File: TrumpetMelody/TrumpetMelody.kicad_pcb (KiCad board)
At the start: 2 copper layers, 76.2 x 68.6 mm, 81 parts, among them J1 USB_B_Micro, J2 Conn_01x05, J3 640456-3, J4 640456-3, SW1 SW_Push, U1 STM32F411RETx, U2 TLV62565DBVR, U3 MAX98357AETE_T, U4 MAX7375AXR805

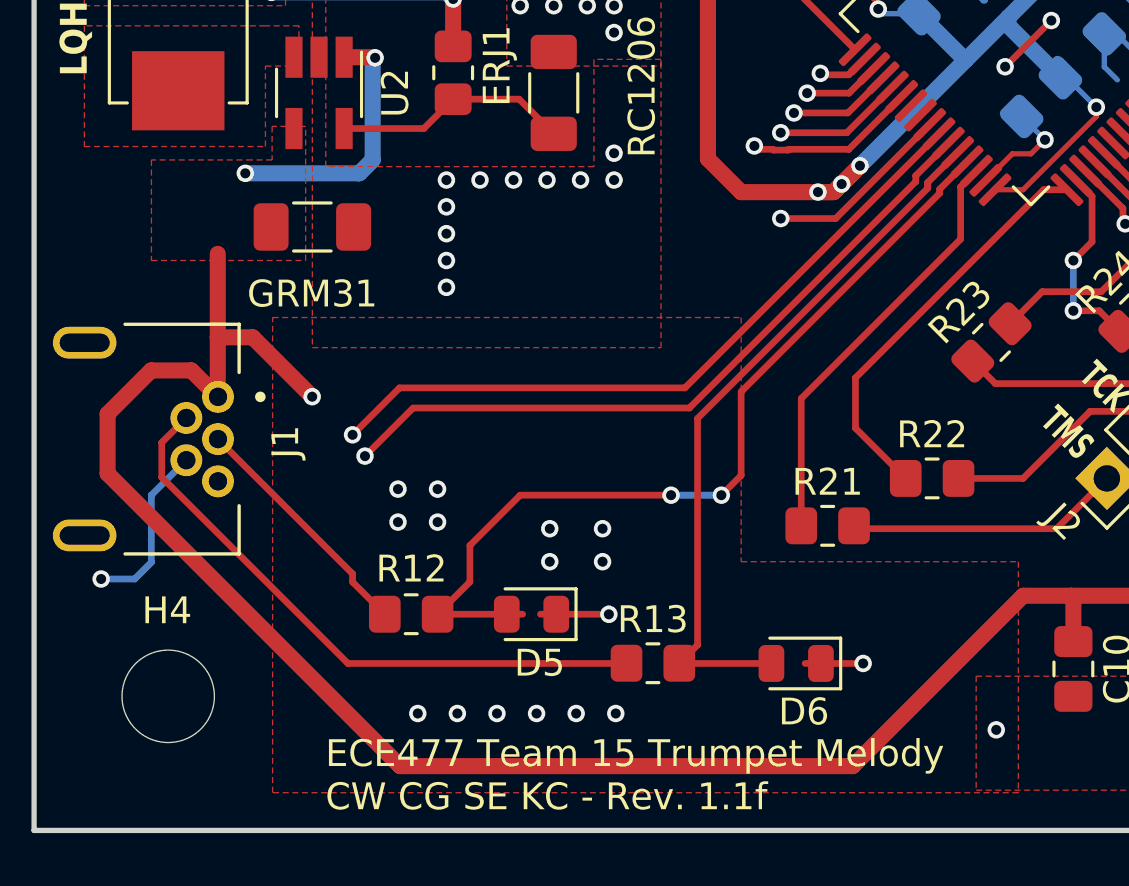
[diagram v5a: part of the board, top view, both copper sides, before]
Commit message: New ESD protection on USB and verified
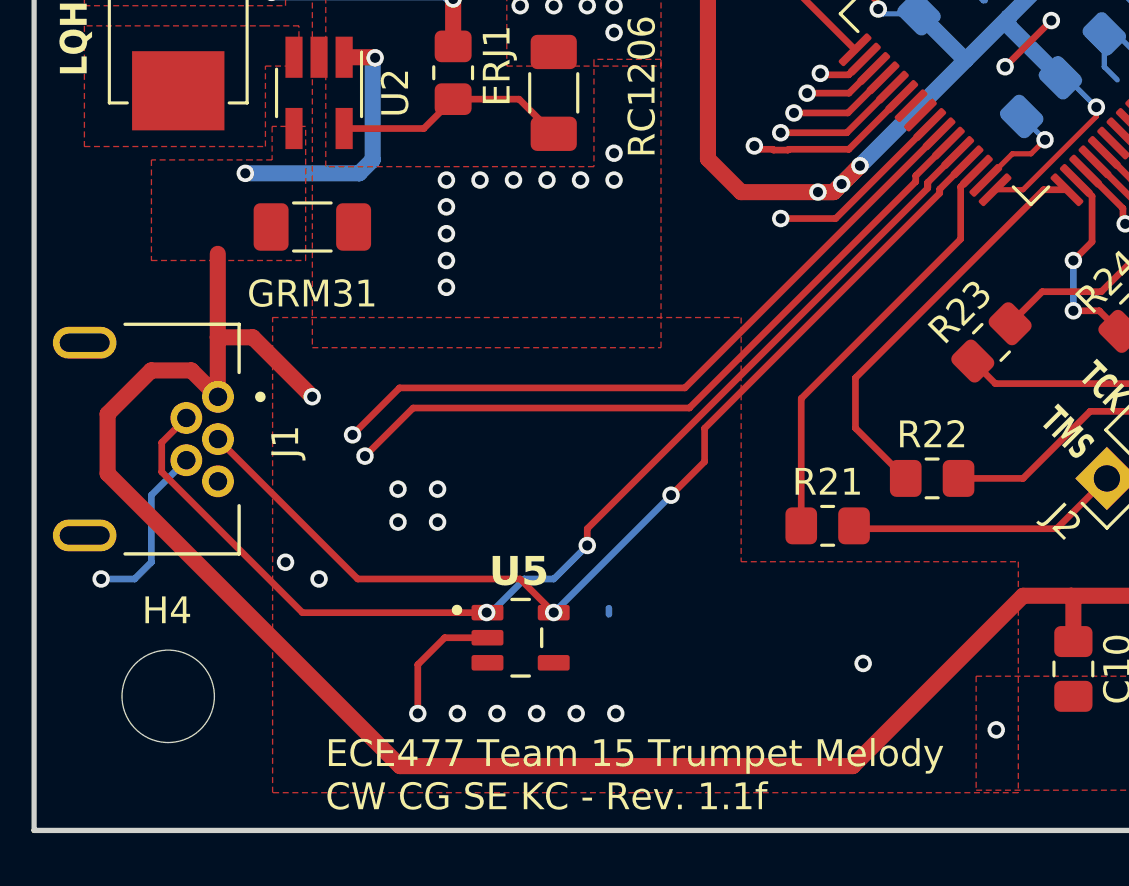
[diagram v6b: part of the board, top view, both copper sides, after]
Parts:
- removed D5, D6: D_TVS, Diode_SMD:D_0805_2012Metric
- removed R12, R13: 220, Resistor_SMD:R_0805_2012Metric_Pad1.20x1.40mm_HandSolder
- added U5: ESDS304DBVR, TrumpetMelodyFootprintLibrary:SOT95P280X145-5N, F.Cu at (165.8, 107.0)
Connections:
- J1 pad 2: Net-(J1-D-) -> USB_DM
- J1 pad 3: Net-(J1-D+) -> USB_DP
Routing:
- net Net-(J1-D-): track 23.6 -> 0.00 mm
- net USB_DM: track 27.4 -> 42.8 mm, vias 0 -> 2
- net Net-(J1-D+): track 9.26 -> 0.00 mm
- net USB_DP: track 33.1 -> 39.0 mm
- net GND: track 54.6 -> 54.7 mm, vias 146 -> 143

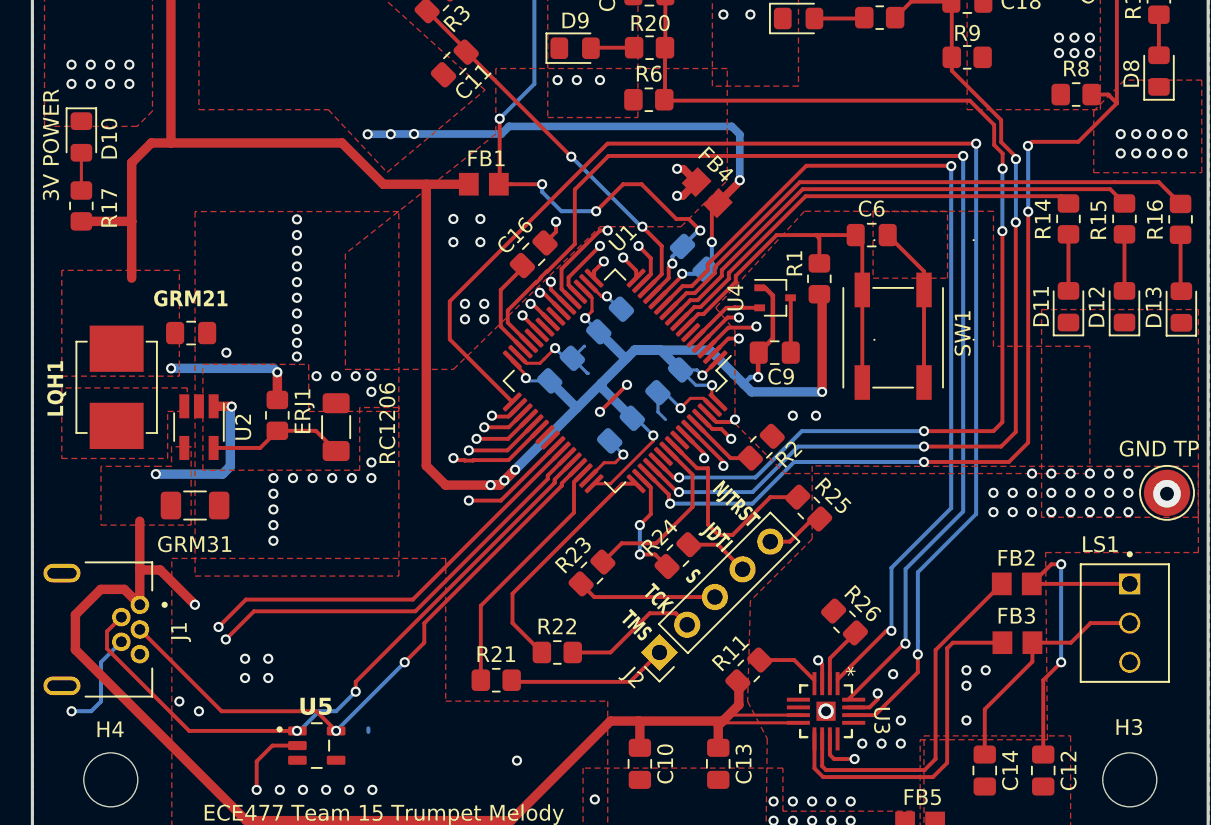
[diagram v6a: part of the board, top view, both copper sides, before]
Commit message: changes to DP/DM signals to reduce via usage/turns, slight change to the button 0 routing bc i saw an acute angle
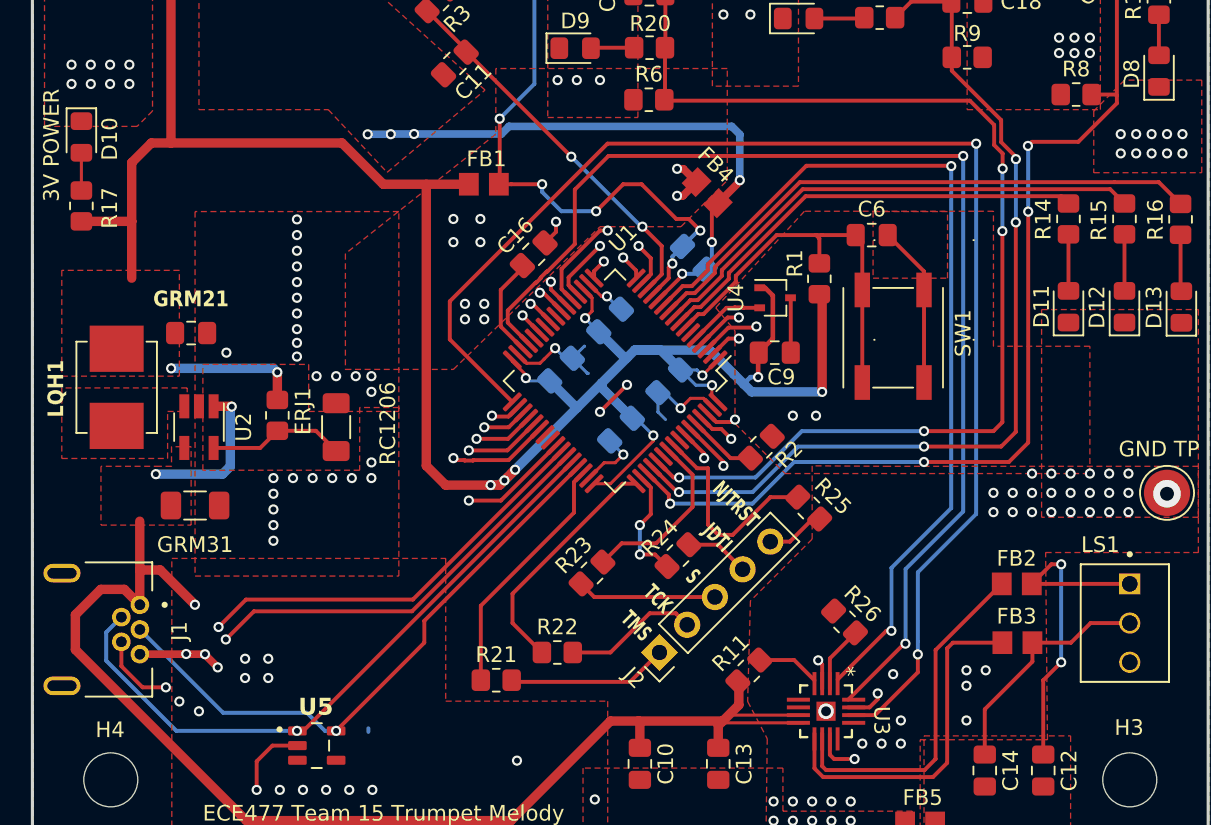
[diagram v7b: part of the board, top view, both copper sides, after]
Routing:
- net GND: track 54.7 -> 60.1 mm, vias 143 -> 146
- net USB_ID_Connector: track 6.58 -> 5.03 mm
- net USB_DM: track 42.8 -> 42.7 mm, vias 2 -> 1
- net USB_DP: vias 2 -> 1
